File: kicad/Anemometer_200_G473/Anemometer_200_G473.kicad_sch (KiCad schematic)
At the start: 146 parts, among them J1 Conn_01x01_Female, J11 USB_B_Micro, J13 Conn_01x01_Female, J15 Conn_01x01_Female, J16 Conn_01x01_Female, J17 Conn_01x01_Female, J2 Conn_01x01_Female, J20 Conn_01x01_Female, J21 Conn_01x01_Female, J22 Conn_01x01_Female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

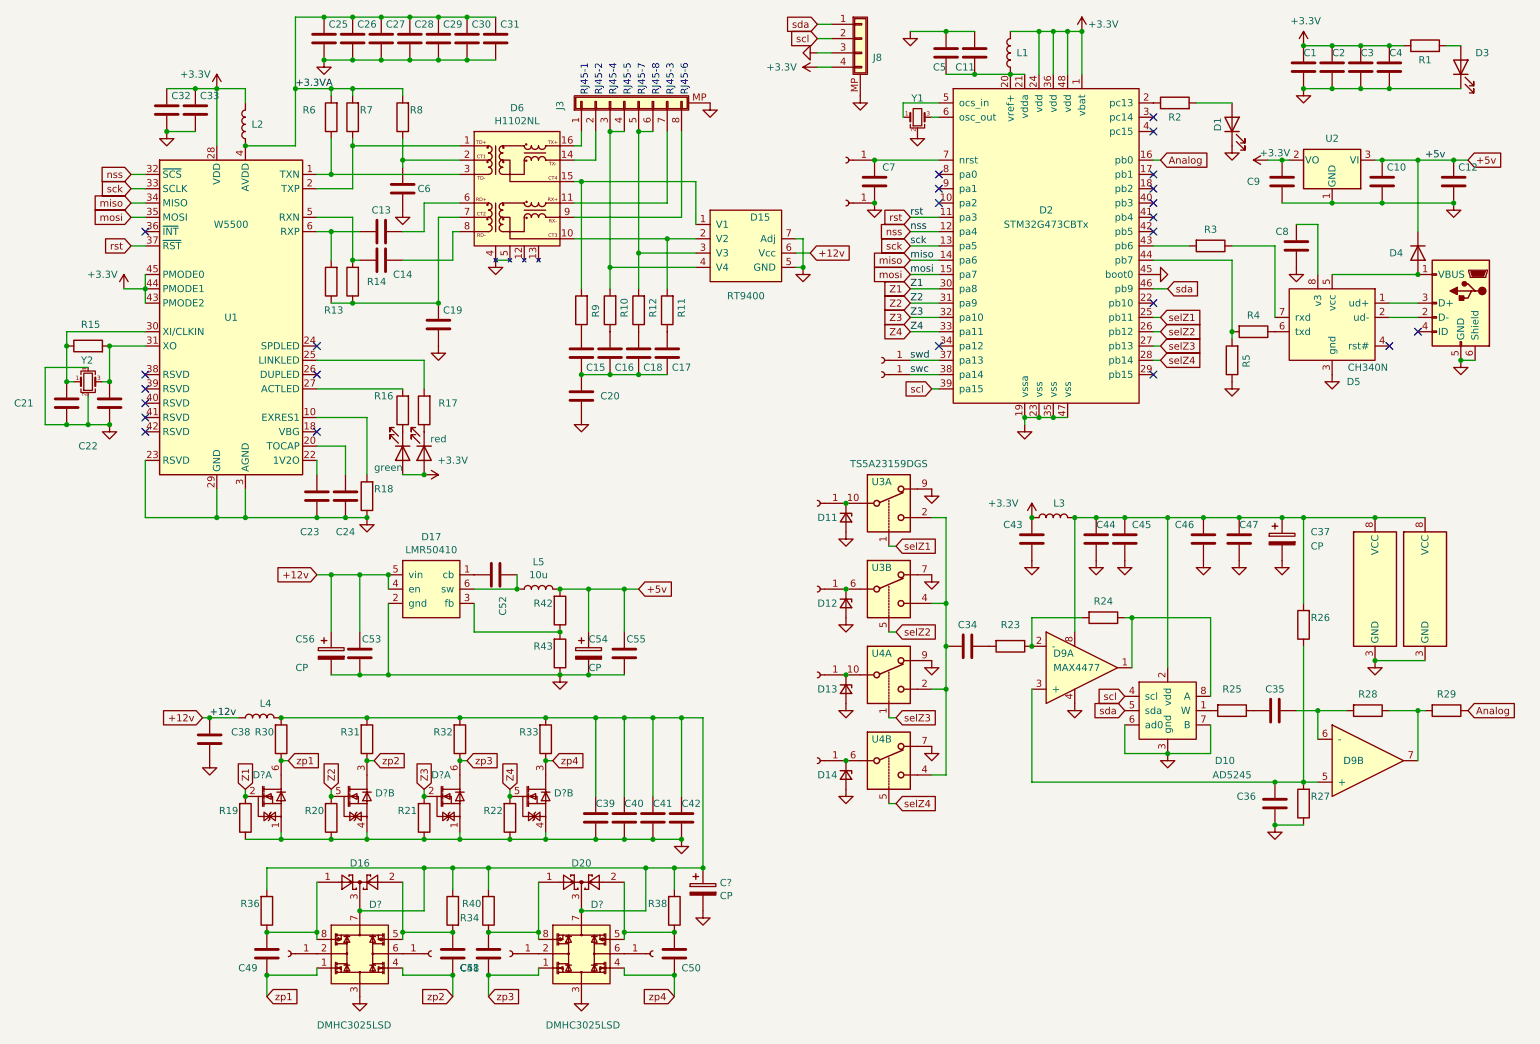
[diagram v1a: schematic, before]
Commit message: изменено:      kicad/Amp200_2/Amp200-rescue.lib 	изменено:      kicad/Anemometer_200_G473/Anemometer_200_G473.kicad_pcb 	изменено:      kicad/Anemometer_200_G473/Anemometer_200_G473.kicad_prl 	изменено:      kicad/Anemometer_200_G473/Anemometer_200_G473.kicad_sch 	изменено:      kicad/Anemometer_200_G473/fp-info-cache 	изменено:      kicad/Anemometr_v3/Anemometr-rescue.lib
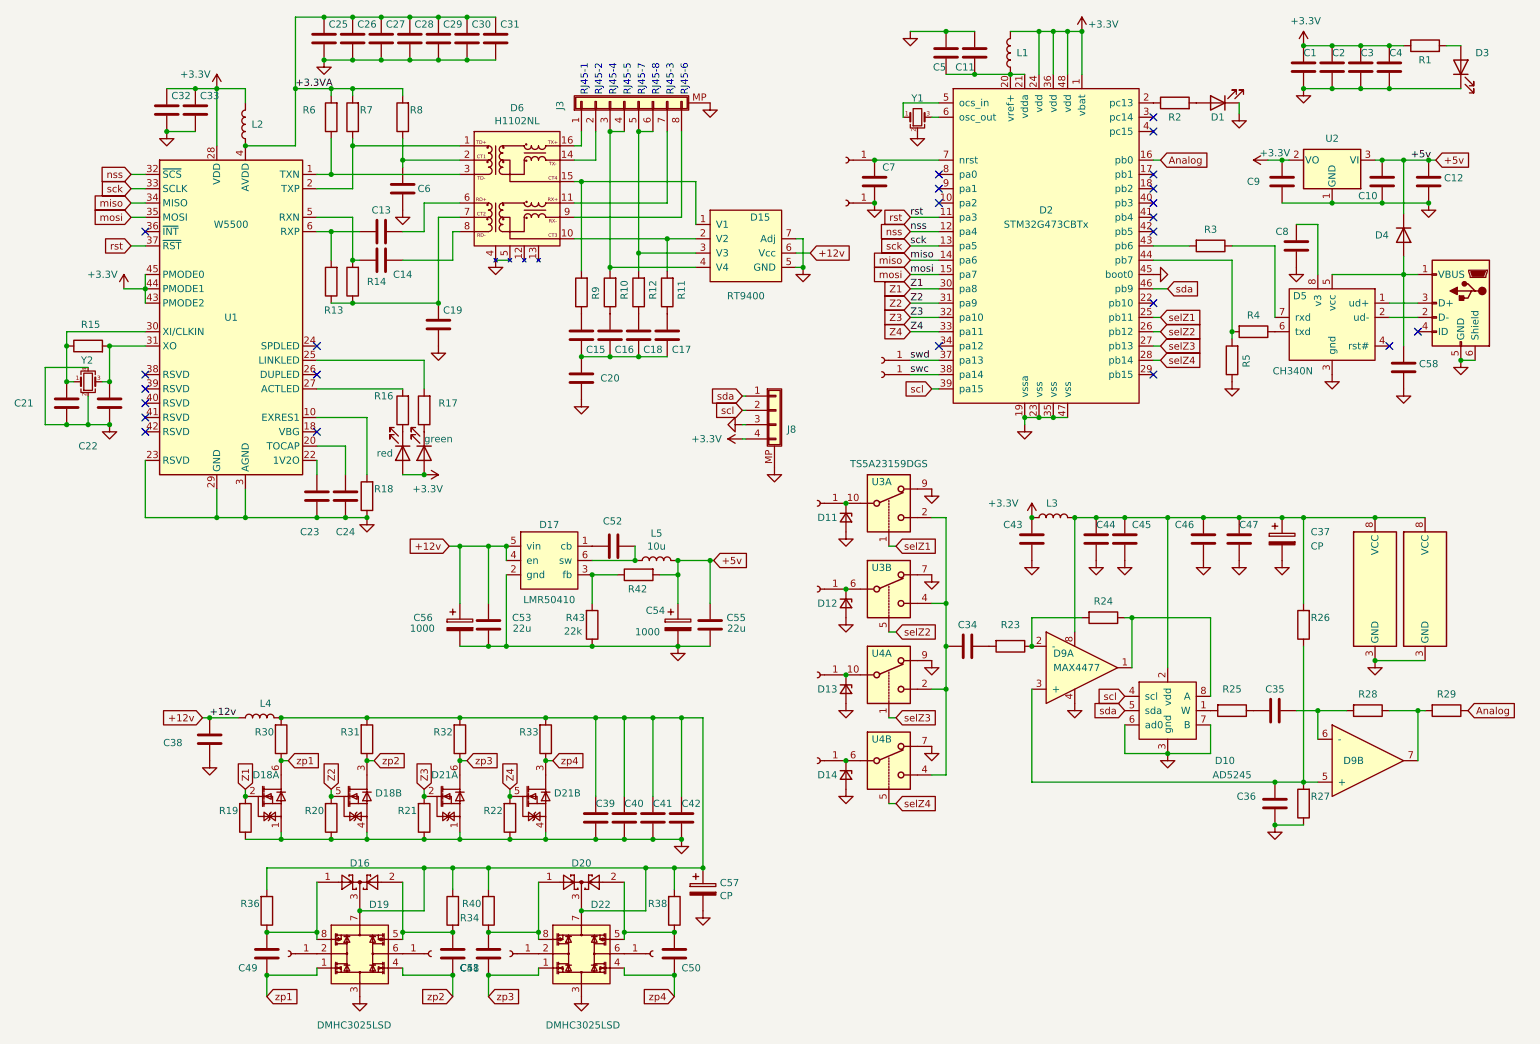
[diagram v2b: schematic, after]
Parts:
- added C58: C, Capacitor_SMD:C_0805_2012Metric, symbol Device:C
- C53, C55: value C -> 22u
- C54, C56: value CP -> 1000
- D10, D9: footprint (none) -> Package_SO:MSOP-8_3x3mm_P0.65mm
- D11, D12, D13, D14: footprint (none) -> Diode_SMD:D_SOD-123
- D15: footprint My-library:TR9400 -> lib:TR9400
- D7: value green -> red
- D8: value red -> green
- J1, J13, J15, J16, J17, J2, J20, J21, J22, J23, J24: footprint My-library:mini_conn -> lib:conn_mini
- J4: renamed from J?; footprint My-library:mini_conn -> lib:conn_mini
- R19, R20, R21, R22: value 12.4k -> 100k
- R30, R31, R32, R33: value 12.4k -> 100
- R43: value 12.4k -> 22k
- Y2: value Crystal_GND24_Small -> 25MHz
- gave numbers to parts that had none: 5
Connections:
- net GND: now also C58.2
- net at D4.2 (A), D5.5 (vcc), J11.1 (VBUS): now also C58.1
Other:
- moved on the sheet: C12, C15, C16, C17, C18, C20, C52, C53, C54, C55, C56, D1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
